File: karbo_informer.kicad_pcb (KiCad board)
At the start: 2 copper layers, 12 parts, among them IC1 MAX7219, IC2 MAX7219, P1 USB_OTG

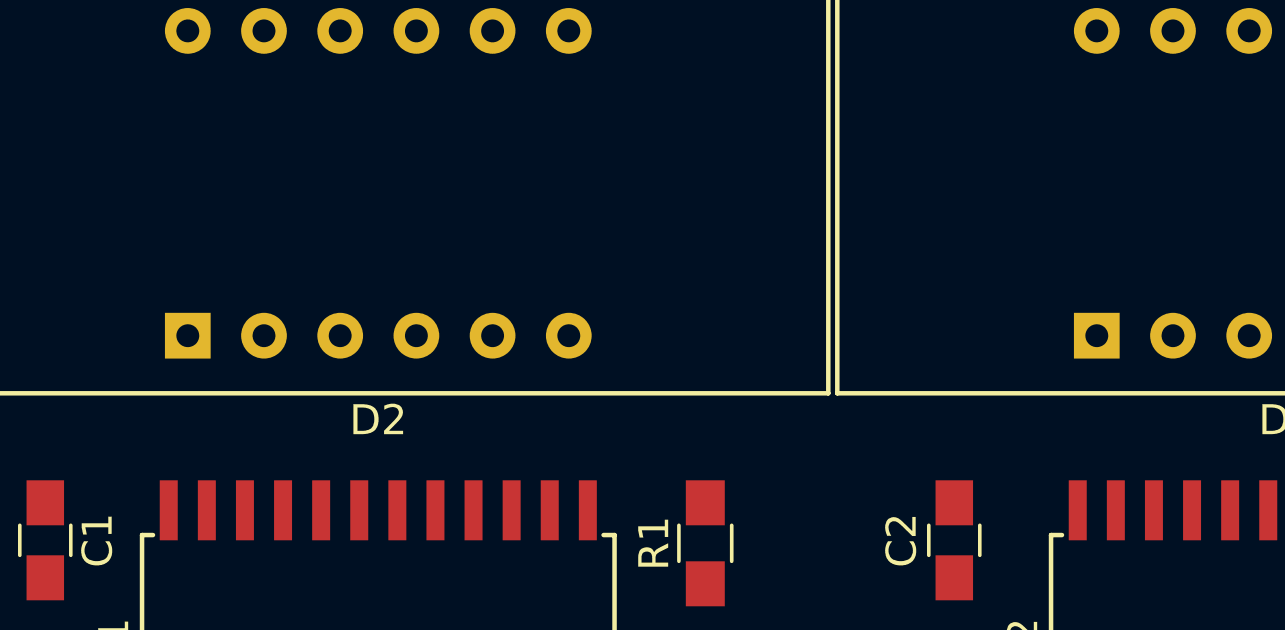
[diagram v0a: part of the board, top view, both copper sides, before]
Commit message: Wire for segmant C (D2 to D4)
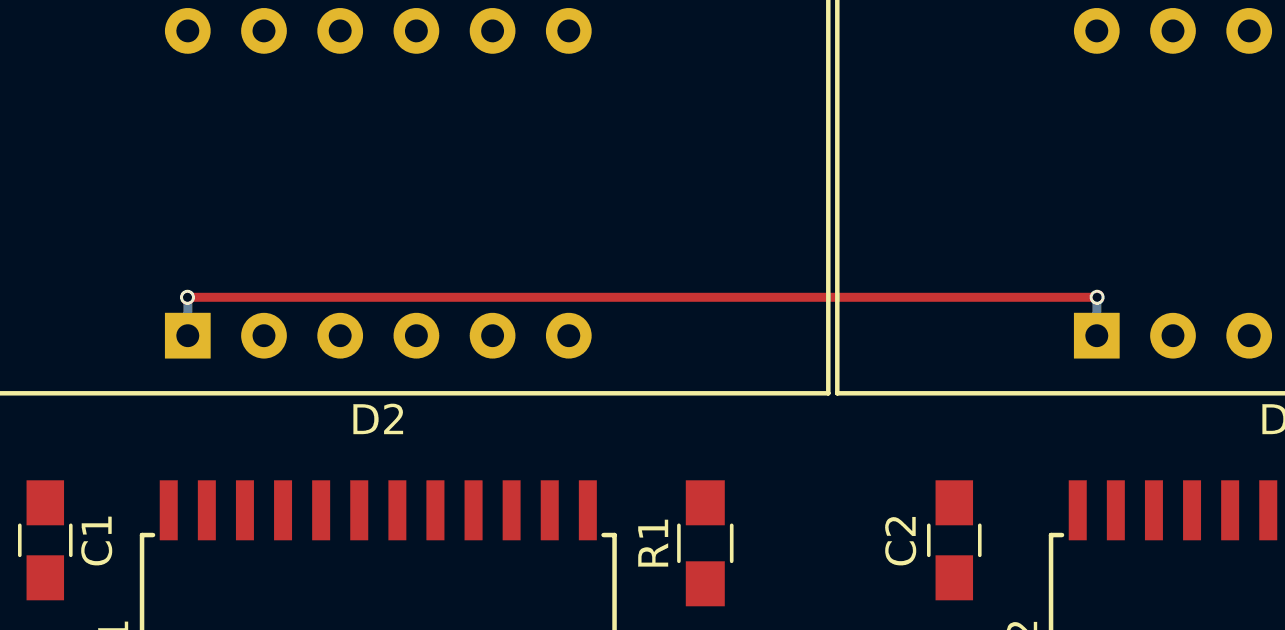
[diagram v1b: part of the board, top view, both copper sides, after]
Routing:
- net /S_SEG_E: track 0.00 -> 32.9 mm, vias 0 -> 2
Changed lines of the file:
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@@
   (general
     (links 69)
-    (no_connects 61)
+    (no_connects 60)
     (area 0 0 0 0)
     (thickness 1.6)
     (drawings 0)
-    (tracks 63)
+    (tracks 69)
     (zones 0)
     (modules 12)
@@
   (segment (start 77.45 23.82) (end 77.45 25.3) (width 0.3) (layer B.Cu) (net 12))
   (segment (start 77.45 25.3) (end 77.45 25.35) (width 0.3) (layer B.Cu) (net 12))
+  (segment (start 34.45 48.28) (end 34.45 47.01) (width 0.3) (layer B.Cu) (net 13) (status 400000))
+  (segment (start 64.75 47.01) (end 64.75 48.28) (width 0.3) (layer B.Cu) (net 13) (status 800000))
+  (segment (start 64.76 47) (end 64.75 47.01) (width 0.3) (layer B.Cu) (net 13))
+  (via (at 64.76 47) (size 0.5) (drill 0.3) (layers F.Cu B.Cu) (net 13))
+  (segment (start 34.44 47) (end 64.76 47) (width 0.3) (layer F.Cu) (net 13))
+  (via (at 34.44 47) (size 0.5) (drill 0.3) (layers F.Cu B.Cu) (net 13))
 )

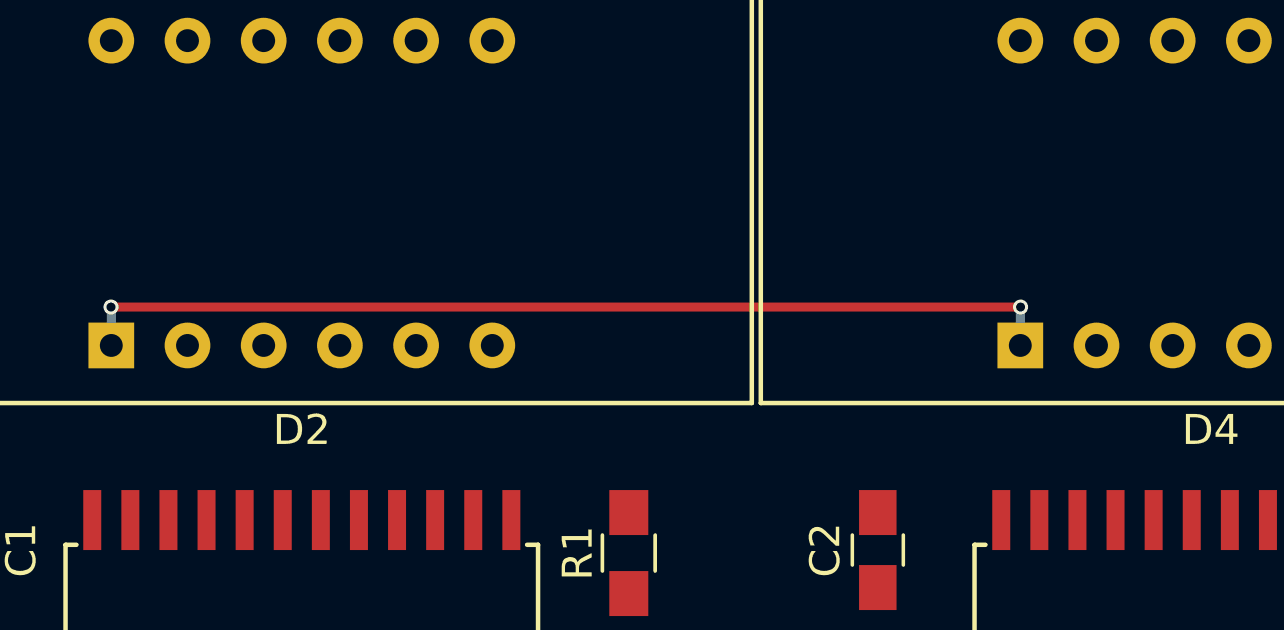
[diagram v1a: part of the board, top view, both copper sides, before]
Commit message: Wire for segmant D (D2 to D4)
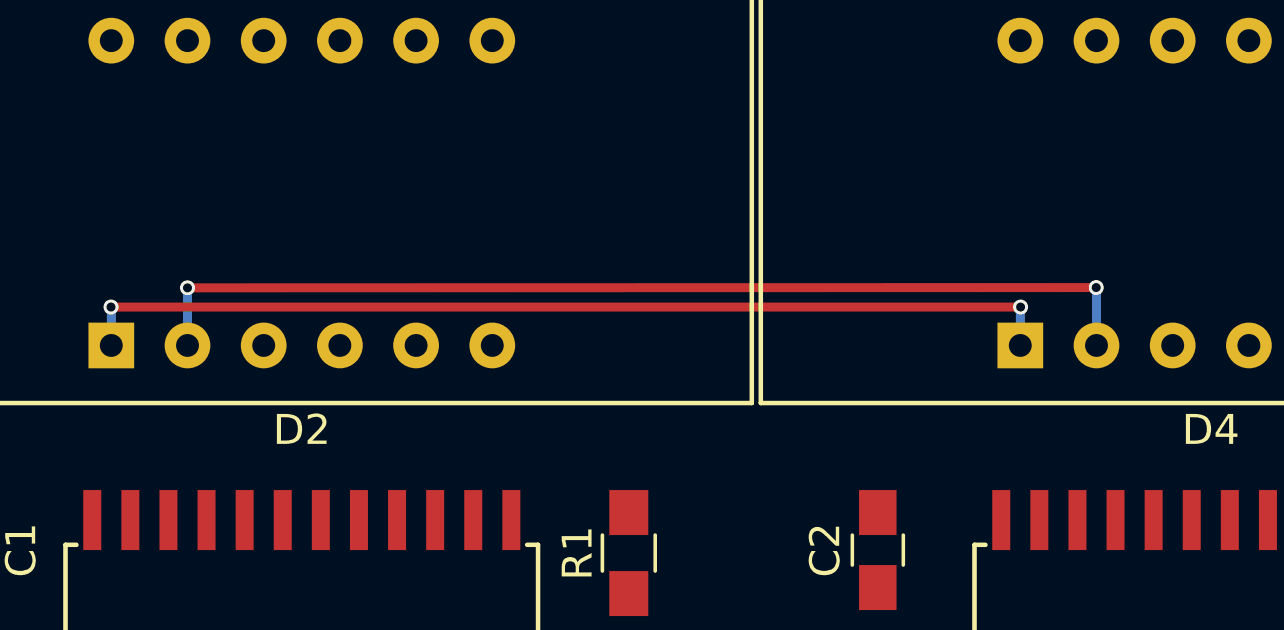
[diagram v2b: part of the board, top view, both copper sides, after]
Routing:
- net /S_SEG_D: track 0.00 -> 34.1 mm, vias 0 -> 2
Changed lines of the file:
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@@
   (general
     (links 69)
-    (no_connects 60)
+    (no_connects 59)
     (area 0 0 0 0)
     (thickness 1.6)
     (drawings 0)
-    (tracks 69)
+    (tracks 74)
     (zones 0)
     (modules 12)
@@
   (segment (start 77.45 23.82) (end 77.45 25.3) (width 0.3) (layer B.Cu) (net 12))
   (segment (start 77.45 25.3) (end 77.45 25.35) (width 0.3) (layer B.Cu) (net 12))
-  (segment (start 34.45 48.28) (end 34.45 47.01) (width 0.3) (layer B.Cu) (net 13) (status 400000))
-  (segment (start 64.75 47.01) (end 64.75 48.28) (width 0.3) (layer B.Cu) (net 13) (status 800000))
+  (segment (start 34.45 48.28) (end 34.45 47.01) (width 0.3) (layer B.Cu) (net 13))
+  (segment (start 64.75 47.01) (end 64.75 48.28) (width 0.3) (layer B.Cu) (net 13))
   (segment (start 64.76 47) (end 64.75 47.01) (width 0.3) (layer B.Cu) (net 13))
   (via (at 64.76 47) (size 0.5) (drill 0.3) (layers F.Cu B.Cu) (net 13))
   (segment (start 34.44 47) (end 64.76 47) (width 0.3) (layer F.Cu) (net 13))
   (via (at 34.44 47) (size 0.5) (drill 0.3) (layers F.Cu B.Cu) (net 13))
+  (via (at 36.99 46.36) (size 0.5) (drill 0.3) (layers F.Cu B.Cu) (net 15))
+  (via (at 67.28 46.35) (size 0.5) (drill 0.3) (layers F.Cu B.Cu) (net 15))
+  (segment (start 67.28 46.35) (end 36.99 46.36) (width 0.3) (layer F.Cu) (net 15))
+  (segment (start 36.99 46.36) (end 36.99 48.28) (width 0.3) (layer B.Cu) (net 15) (status 800000))
+  (segment (start 67.29 46.36) (end 67.29 48.28) (width 0.3) (layer B.Cu) (net 15))
 )

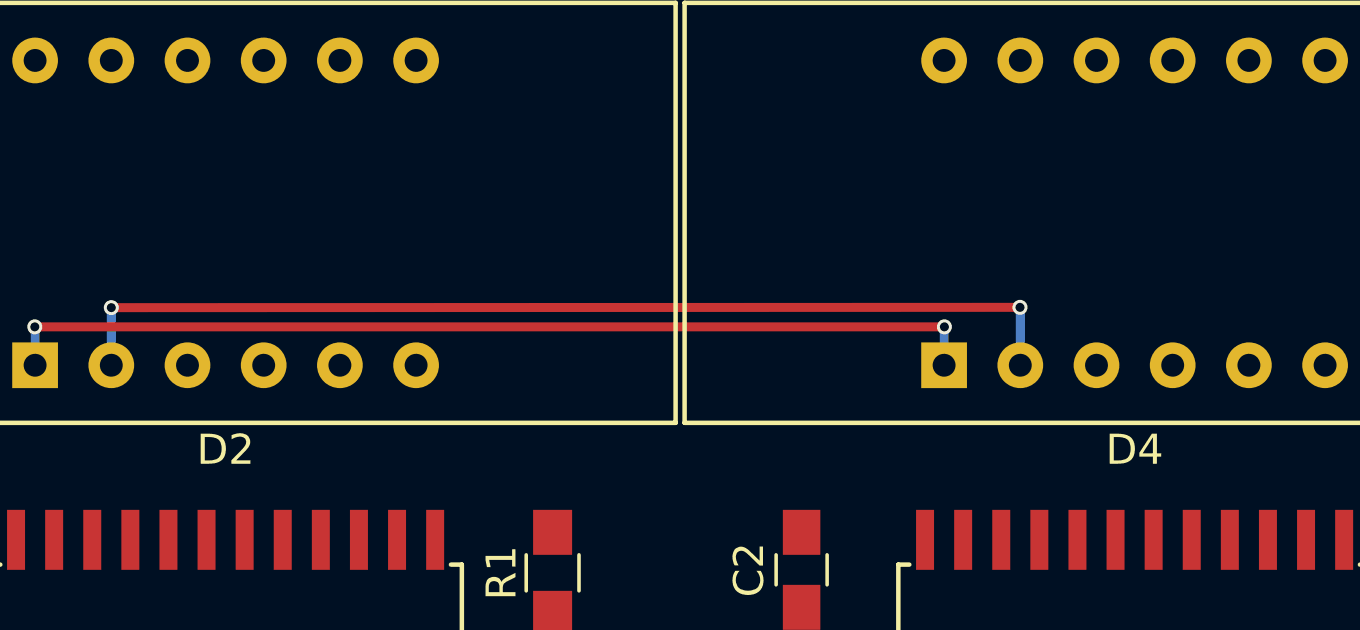
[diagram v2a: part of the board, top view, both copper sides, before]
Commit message: Wire for segments C and DP in the sell line (D2 to D4)
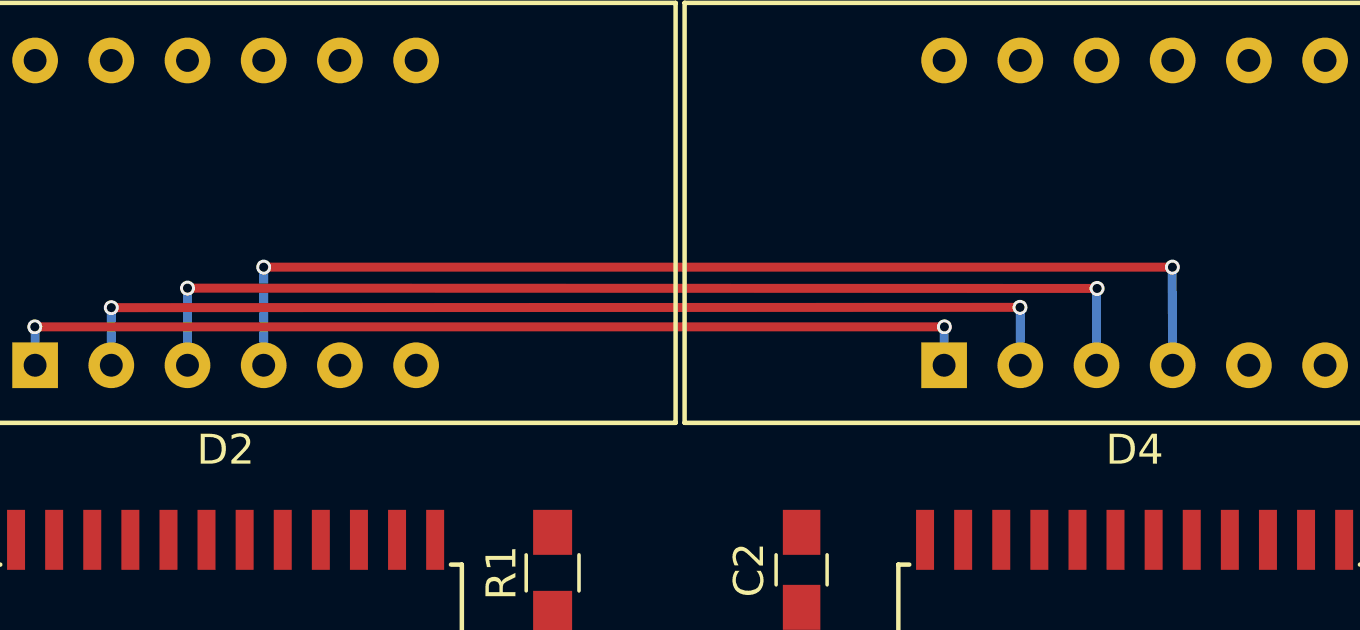
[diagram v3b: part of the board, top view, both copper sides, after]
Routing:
- net /S_SEG_C: track 0.00 -> 36.8 mm, vias 0 -> 2
- net /S_SEG_DP: track 0.00 -> 35.5 mm, vias 0 -> 2
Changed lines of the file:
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@@
   (general
     (links 69)
-    (no_connects 59)
+    (no_connects 57)
     (area 0 0 0 0)
     (thickness 1.6)
     (drawings 0)
-    (tracks 74)
+    (tracks 85)
     (zones 0)
     (modules 12)
@@
   (segment (start 34.44 47) (end 64.76 47) (width 0.3) (layer F.Cu) (net 13))
   (via (at 34.44 47) (size 0.5) (drill 0.3) (layers F.Cu B.Cu) (net 13))
+  (via (at 39.53 45.71) (size 0.5) (drill 0.3) (layers F.Cu B.Cu) (net 14))
+  (segment (start 39.53 45.71) (end 69.85 45.72) (width 0.3) (layer F.Cu) (net 14))
+  (via (at 69.85 45.72) (size 0.5) (drill 0.3) (layers F.Cu B.Cu) (net 14))
+  (segment (start 69.85 45.72) (end 69.83 45.74) (width 0.3) (layer B.Cu) (net 14))
+  (segment (start 69.83 48.28) (end 69.83 45.74) (width 0.3) (layer B.Cu) (net 14) (status 400000))
+  (segment (start 39.53 45.71) (end 39.53 48.3) (width 0.3) (layer B.Cu) (net 14))
   (via (at 36.99 46.36) (size 0.5) (drill 0.3) (layers F.Cu B.Cu) (net 15))
   (via (at 67.28 46.35) (size 0.5) (drill 0.3) (layers F.Cu B.Cu) (net 15))
@@
   (segment (start 36.99 46.36) (end 36.99 48.28) (width 0.3) (layer B.Cu) (net 15) (status 800000))
   (segment (start 67.29 46.36) (end 67.29 48.28) (width 0.3) (layer B.Cu) (net 15))
+  (via (at 42.07 45.01) (size 0.5) (drill 0.3) (layers F.Cu B.Cu) (net 16))
+  (segment (start 42.07 48.28) (end 42.07 45.01) (width 0.3) (layer B.Cu) (net 16) (status 400000))
+  (segment (start 72.35 45.02) (end 72.37 48.28) (width 0.3) (layer B.Cu) (net 16) (status 800000))
+  (via (at 72.36 45.01) (size 0.5) (drill 0.3) (layers F.Cu B.Cu) (net 16))
+  (segment (start 42.07 45.01) (end 72.36 45.01) (width 0.3) (layer F.Cu) (net 16))
 )

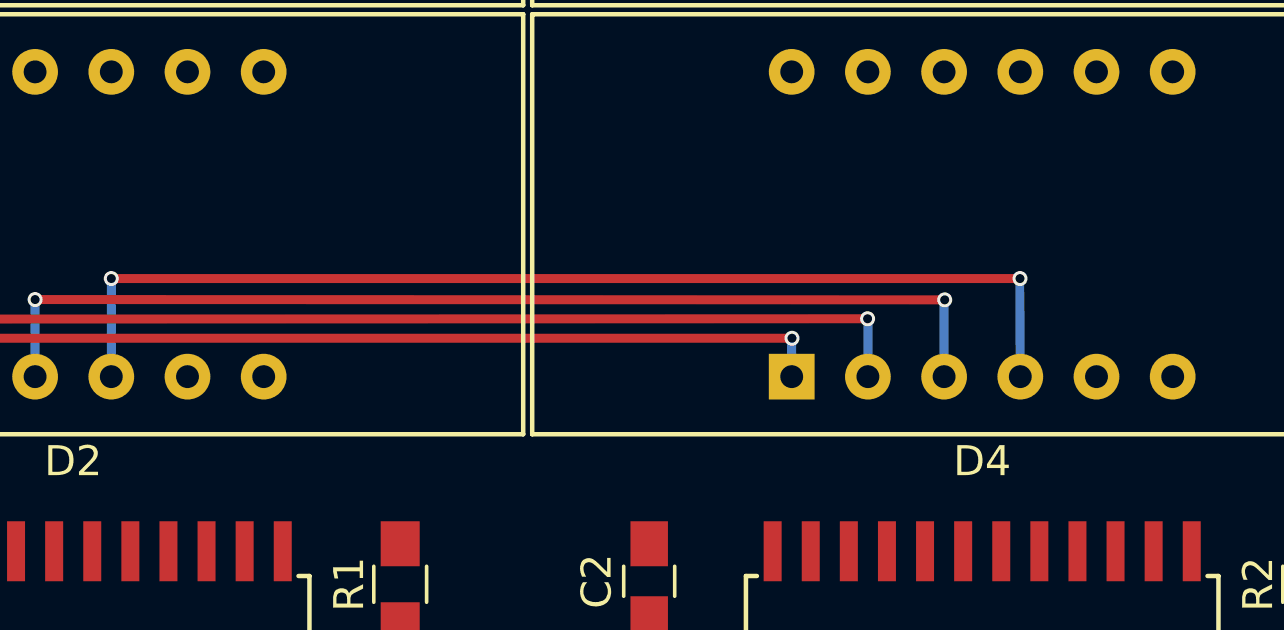
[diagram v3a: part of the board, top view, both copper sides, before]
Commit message: Wire for segments G in the sell line (D2 to D4)
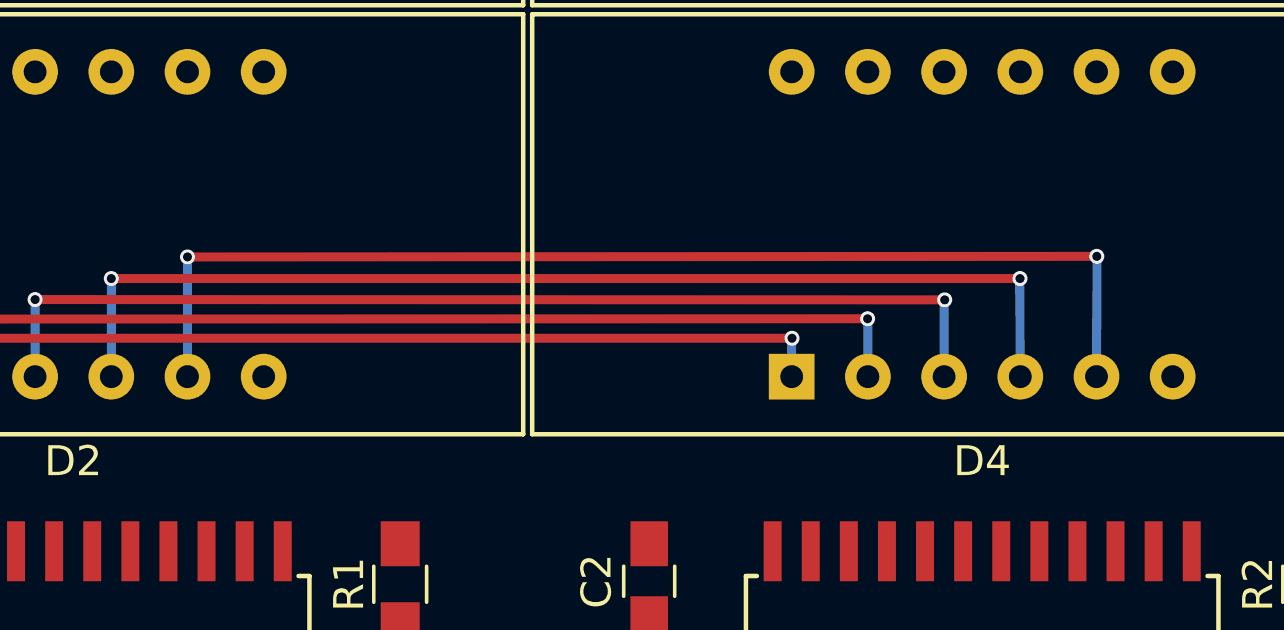
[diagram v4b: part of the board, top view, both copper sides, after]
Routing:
- net /S_SEG_G: track 0.00 -> 38.3 mm, vias 0 -> 2
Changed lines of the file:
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@@
   (general
     (links 69)
-    (no_connects 57)
+    (no_connects 56)
     (area 0 0 0 0)
     (thickness 1.6)
     (drawings 0)
-    (tracks 85)
+    (tracks 90)
     (zones 0)
     (modules 12)
@@
   (via (at 72.36 45.01) (size 0.5) (drill 0.3) (layers F.Cu B.Cu) (net 16))
   (segment (start 42.07 45.01) (end 72.36 45.01) (width 0.3) (layer F.Cu) (net 16))
+  (segment (start 44.61 48.28) (end 44.61 44.29) (width 0.3) (layer B.Cu) (net 17) (status 400000))
+  (segment (start 74.93 44.28) (end 74.91 48.28) (width 0.3) (layer B.Cu) (net 17) (status 800000))
+  (via (at 74.92 44.27) (size 0.5) (drill 0.3) (layers F.Cu B.Cu) (net 17))
+  (segment (start 44.62 44.29) (end 74.92 44.27) (width 0.3) (layer F.Cu) (net 17))
+  (via (at 44.61 44.29) (size 0.5) (drill 0.3) (layers F.Cu B.Cu) (net 17))
 )
